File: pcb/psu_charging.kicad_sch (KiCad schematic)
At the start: 26 parts, among them J4 VBUS, J5 Conn_01x02_Pin, J7 GND, J8 124018612112A, U1 AP2112K-3.3, U4 MCP73831/OT

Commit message: Updated footprints try to fix DRC
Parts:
- J5, JP2: now left out of the parts list
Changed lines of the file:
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@@
   )
   (symbol (lib_id "Jumper:Jumper_2_Bridged") (at 106.68 35.56 180) (unit 1)
-    (in_bom yes) (on_board yes) (dnp no) (fields_autoplaced)
+    (in_bom no) (on_board yes) (dnp no) (fields_autoplaced)
     (property "Reference" "JP2" (at 106.68 30.48 0)
       (effects (font (size 1.27 1.27)))
@@
   )
   (symbol (lib_id "Connector:Conn_01x02_Pin") (at 107.95 40.64 270) (unit 1)
-    (in_bom yes) (on_board yes) (dnp no)
+    (in_bom no) (on_board yes) (dnp no)
     (property "Reference" "J5" (at 105.41 38.1 90)
       (effects (font (size 1.27 1.27)) (justify left))

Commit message: Mark oull-down resistor for EN pin as DNP
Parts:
- R2: value 10k -> 10k/DNP
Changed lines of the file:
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@@
       (effects (font (size 1.27 1.27)) (justify left))
     )
-    (property "Value" "10k" (at 126.492 56.007 0)
+    (property "Value" "10k/DNP" (at 126.492 56.007 0)
       (effects (font (size 1.27 1.27)) (justify left))
     )

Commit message: Add changed pcb files
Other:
- note added: "Change from Voltage-Divider to use one GND of USB"
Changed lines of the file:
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@@
     (effects (font (size 1.27 1.27)) (justify left bottom))
+  )
+  (text "Change from Voltage-Divider \nto use one GND of USB"
+    (at 215.9 146.05 0)
+    (effects (font (size 3 3) (thickness 0.6) bold (color 255 0 0 1)) (justify left bottom))
   )
   (label "VBUS_DETECT" (at 45.72 25.4 180) (fields_autoplaced)

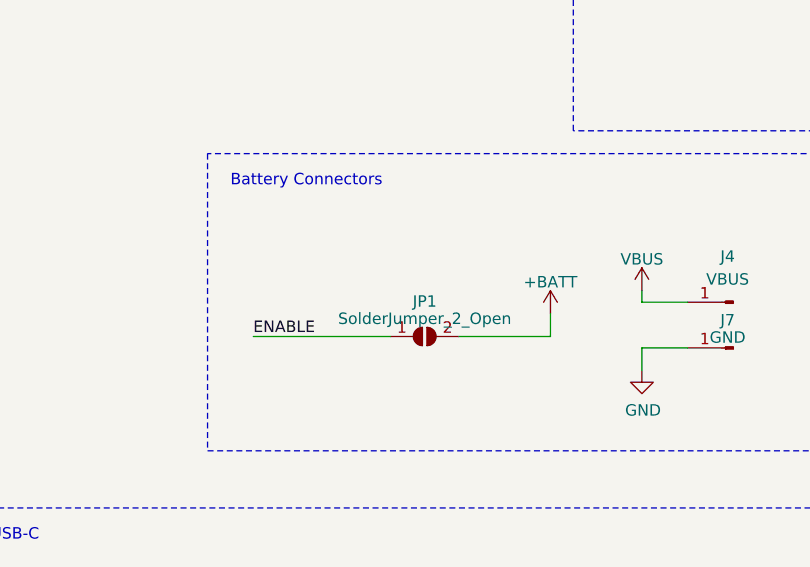
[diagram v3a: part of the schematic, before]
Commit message: Added Testpoints on bottom side
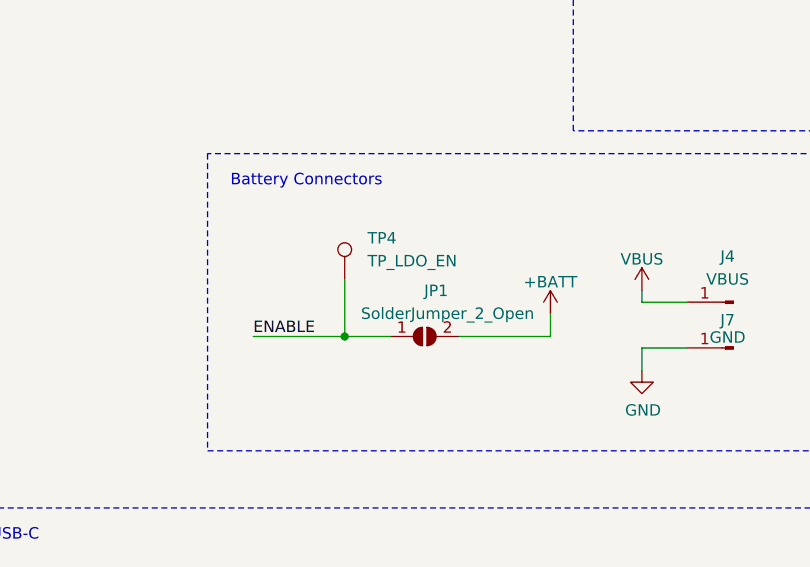
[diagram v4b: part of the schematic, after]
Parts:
- added TP4: TP_LDO_EN, TestPoint:TestPoint_Pad_D1.0mm, symbol Connector:TestPoint
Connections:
- net ENABLE: now also TP4.1
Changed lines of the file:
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@@
   (junction (at 154.94 46.99) (diameter 0) (color 0 0 0 0)
+  )
+  (junction (at 59.69 93.98) (diameter 0) (color 0 0 0 0)
   )
   (junction (at 124.46 46.99) (diameter 0) (color 0 0 0 0)
@@
     (stroke (width 0) (type default))
   )
+  (wire (pts (xy 59.69 93.98) (xy 64.77 93.98))
+    (stroke (width 0) (type default))
+  )
   (wire (pts (xy 68.58 147.32) (xy 80.01 147.32))
     (stroke (width 0) (type default))
@@
     (stroke (width 0) (type default))
   )
+  (wire (pts (xy 59.69 87.63) (xy 59.69 93.98))
+    (stroke (width 0) (type default))
+  )
   (wire (pts (xy 256.54 88.9) (xy 254 88.9))
     (stroke (width 0) (type default))
@@
     (stroke (width 0) (type default))
   )
-  (wire (pts (xy 49.53 93.98) (xy 64.77 93.98))
+  (wire (pts (xy 49.53 93.98) (xy 59.69 93.98))
     (stroke (width 0) (type default))
   )
@@
   )
   (symbol (lib_id "Jumper:SolderJumper_2_Open") (at 68.58 93.98 0) (unit 1)
-    (in_bom no) (on_board yes) (dnp no) (fields_autoplaced)
-    (property "Reference" "JP1" (at 68.58 90.0811 0)
-      (effects (font (size 1.27 1.27)))
-    )
-    (property "Value" "SolderJumper_2_Open" (at 68.58 92.0021 0)
+    (in_bom no) (on_board yes) (dnp no)
+    (property "Reference" "JP1" (at 69.85 88.9 0)
+      (effects (font (size 1.27 1.27)))
+    )
+    (property "Value" "SolderJumper_2_Open" (at 71.12 91.44 0)
       (effects (font (size 1.27 1.27)))
     )
@@
         )
       )
+    )
+  )
+  (symbol (lib_id "Connector:TestPoint") (at 59.69 87.63 0) (unit 1)
+    (in_bom no) (on_board yes) (dnp no) (fields_autoplaced)
+    (property "Reference" "TP4" (at 62.23 83.058 0)
+      (effects (font (size 1.27 1.27)) (justify left))
+    )
+    (property "Value" "TP_LDO_EN" (at 62.23 85.598 0)
+      (effects (font (size 1.27 1.27)) (justify left))
+    )
+    (property "Footprint" "TestPoint:TestPoint_Pad_D1.0mm" (at 64.77 87.63 0)
+      (effects (font (size 1.27 1.27)) hide)
+    )
+    (property "Datasheet" "~" (at 64.77 87.63 0)
+      (effects (font (size 1.27 1.27)) hide)
+    )
+    (pin "1")
+    (instances
+      (project "rep-trap-pcb"
+        (path "/b363dc8f-4a45-4779-a397-ccb82393dab8/eebb1d37-a01d-4adf-be70-a8e8f9293475/571cfc2c-17d3-4043-8736-10f73b37aef8"
+          (reference "TP4") (unit 1)
+        )
+        (path "/b363dc8f-4a45-4779-a397-ccb82393dab8/eebb1d37-a01d-4adf-be70-a8e8f9293475/23008b32-6835-495f-a93f-d60d3125c4cb"
+          (reference "TP14") (unit 1)
+        )
+      )

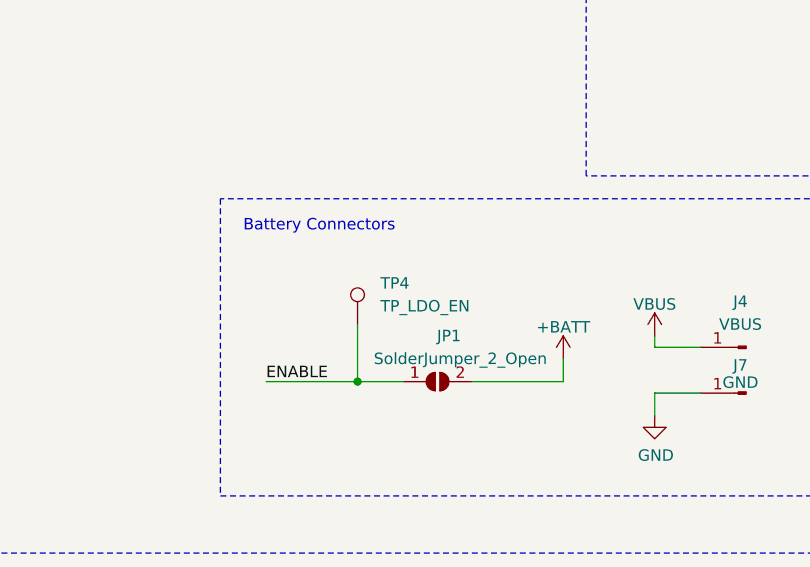
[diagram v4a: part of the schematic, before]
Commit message: Update to use KiCad8
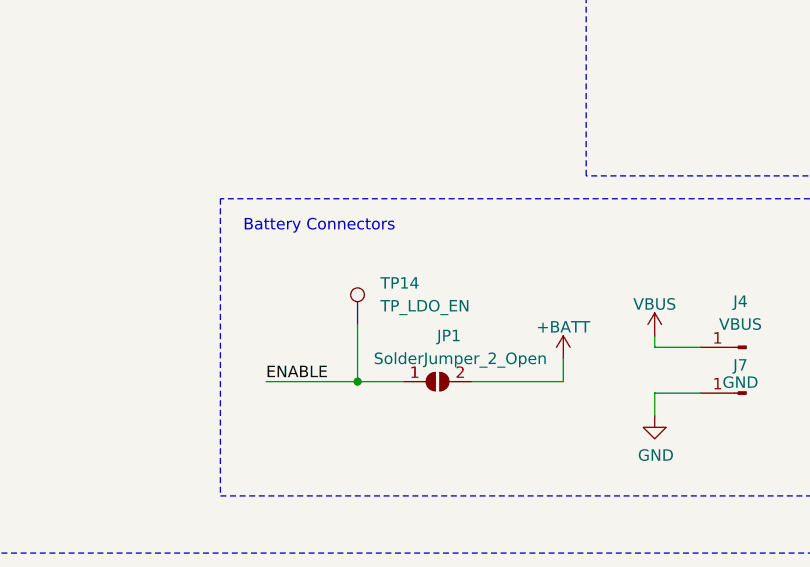
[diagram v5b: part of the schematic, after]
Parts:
- renumbered TP4 to TP14

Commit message: PCB update
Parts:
- BT1: value 1042 -> BH-18650-B1BA002
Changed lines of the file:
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@@
 			)
 		)
-		(property "Value" "1042"
+		(property "Value" "BH-18650-B1BA002"
 			(at 139.7 93.4085 0)
 			(effects
